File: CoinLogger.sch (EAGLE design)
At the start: 18 parts, among them IC1 TINY11S, U4 LIS331, X1 USB-MICROB

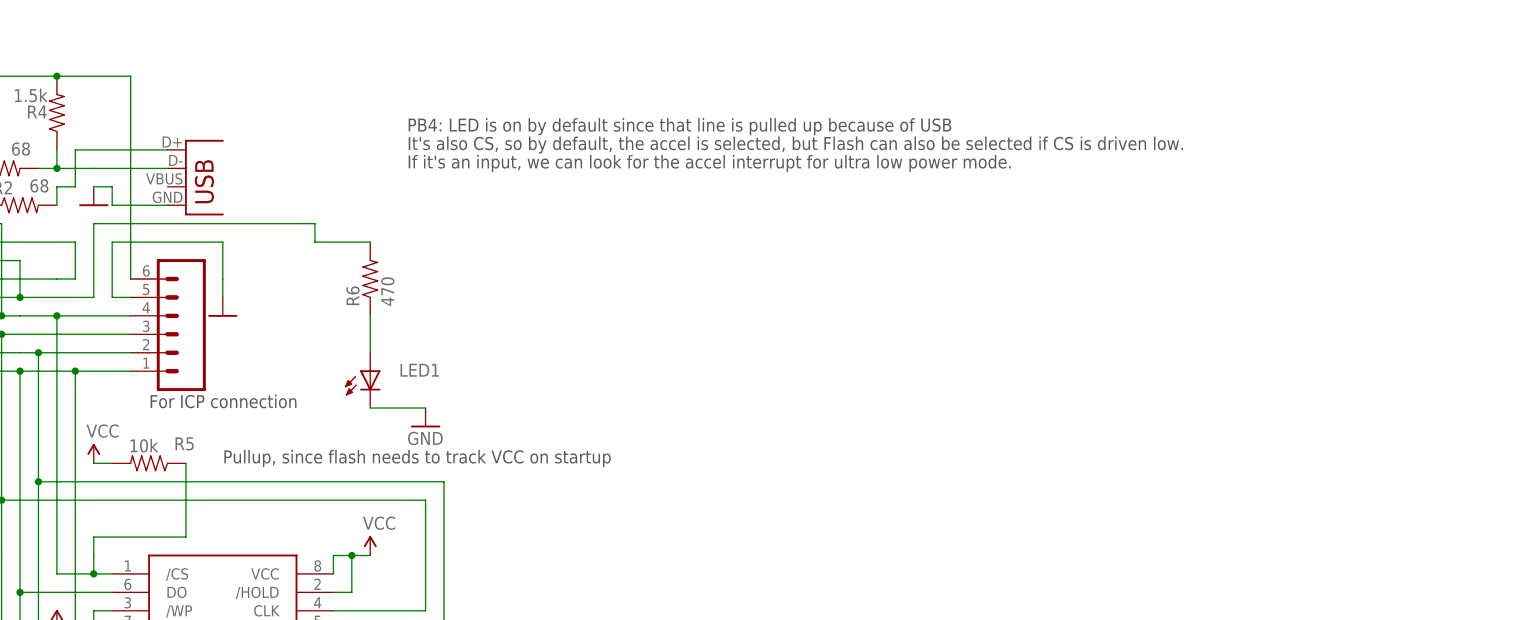
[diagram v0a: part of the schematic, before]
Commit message: Updated and rerouted V1.1, early nanologger layout
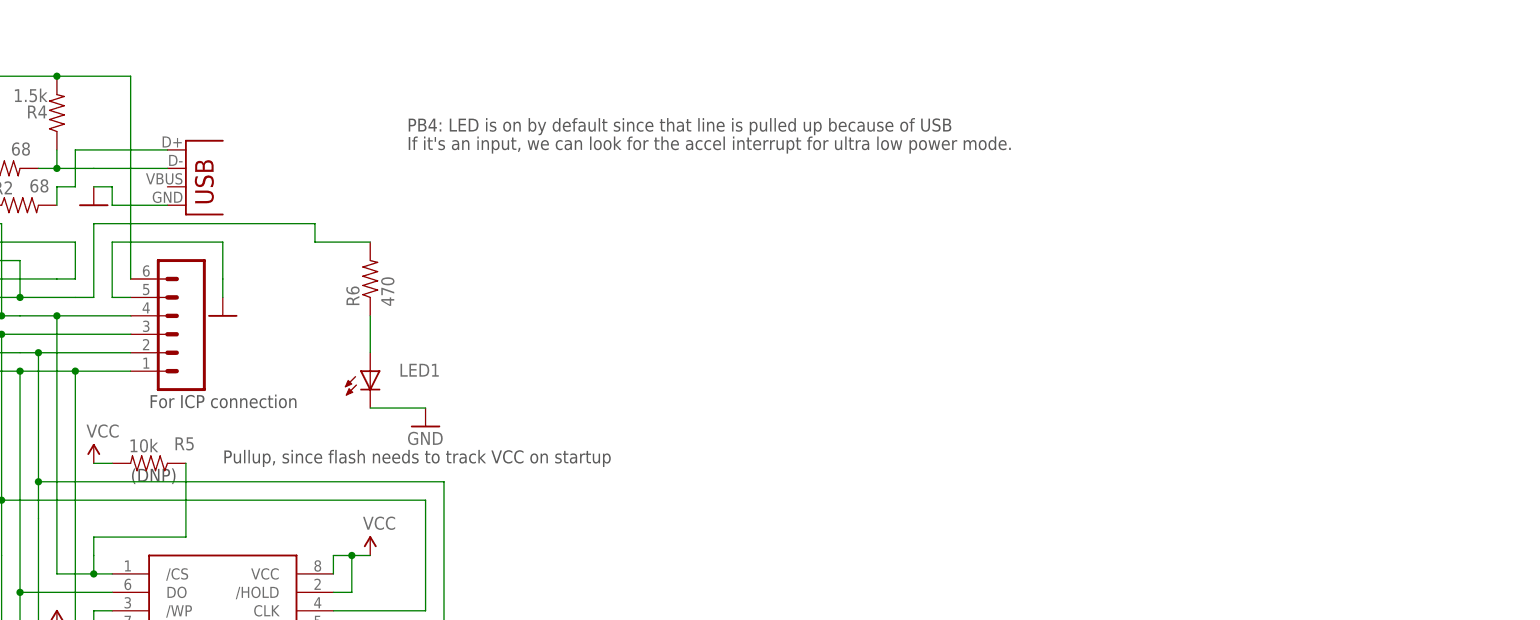
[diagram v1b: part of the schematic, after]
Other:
- note added: "(DNP)"
- note removed: "It's also CS, so by default, the accel is selected, but Flash can also be selected if CS is driven low."
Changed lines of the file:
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@@
 <text x="33.02" y="71.12" size="1.778" layer="97">PB3: CS</text>
 <text x="116.84" y="81.28" size="1.778" layer="97">PB4: LED is on by default since that line is pulled up because of USB</text>
-<text x="116.84" y="78.74" size="1.778" layer="97">It's also CS, so by default, the accel is selected, but Flash can also be selected if CS is driven low.</text>
-<text x="116.84" y="76.2" size="1.778" layer="97">If it's an input, we can look for the accel interrupt for ultra low power mode.</text>
+<text x="116.84" y="78.74" size="1.778" layer="97">If it's an input, we can look for the accel interrupt for ultra low power mode.</text>
+<text x="78.74" y="33.02" size="1.778" layer="97">(DNP)</text>
 </plain>
 <instances>
